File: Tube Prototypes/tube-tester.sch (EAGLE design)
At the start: 32 parts, among them IC1 NE555D, IC2 74141N, IC3 7805, Q1 IRF740S, Q2 BC546

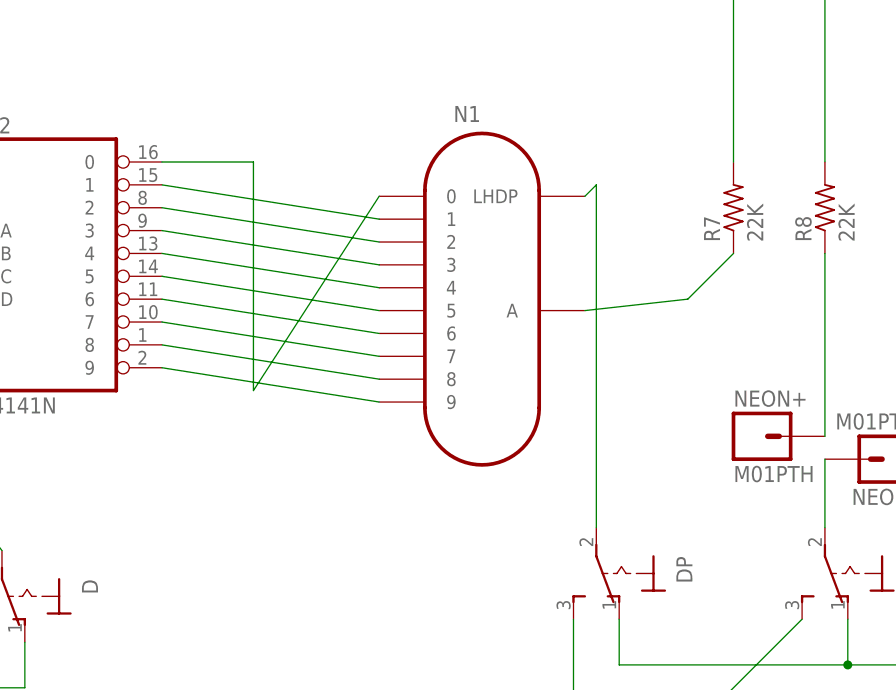
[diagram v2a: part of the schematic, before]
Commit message: new prototype for dual tube board
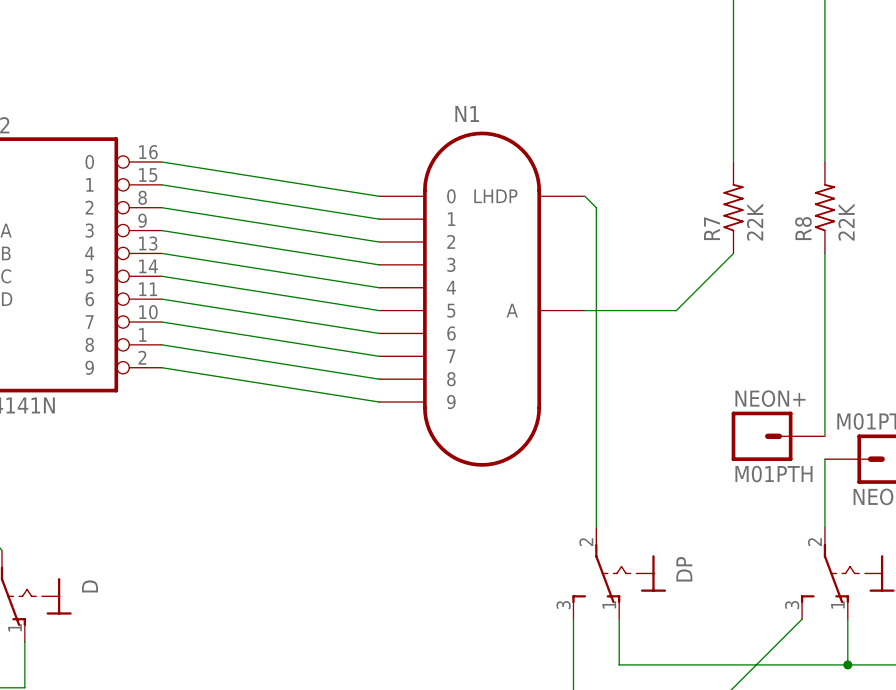
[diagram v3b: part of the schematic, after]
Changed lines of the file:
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@@
 <?xml version="1.0" encoding="utf-8"?>
 <!DOCTYPE eagle SYSTEM "eagle.dtd">
-<eagle version="6.4">
+<eagle version="6.6.0">
 <drawing>
 <settings>
@@
 <grid distance="0.05" unitdist="inch" unit="inch" style="lines" multiple="1" display="yes" altdistance="0.025" altunitdist="inch" altunit="inch"/>
 <layers>
-<layer number="1" name="Top" color="4" fill="1" visible="yes" active="no"/>
-<layer number="2" name="Route2" color="1" fill="3" visible="yes" active="no"/>
-<layer number="3" name="Route3" color="4" fill="3" visible="yes" active="no"/>
-<layer number="14" name="Route14" color="1" fill="6" visible="yes" active="no"/>
-<layer number="15" name="Route15" color="4" fill="6" visible="yes" active="no"/>
-<layer number="16" name="Bottom" color="1" fill="1" visible="yes" active="no"/>
-<layer number="17" name="Pads" color="2" fill="1" visible="yes" active="no"/>
-<layer number="18" name="Vias" color="2" fill="1" visible="yes" active="no"/>
-<layer number="19" name="Unrouted" color="6" fill="1" visible="yes" active="no"/>
-<layer number="20" name="Dimension" color="15" fill="1" visible="yes" active="no"/>
-<layer number="21" name="tPlace" color="7" fill="1" visible="yes" active="no"/>
-<layer number="22" name="bPlace" color="7" fill="1" visible="yes" active="no"/>
-<layer number="23" name="tOrigins" color="15" fill="1" visible="yes" active="no"/>
-<layer number="24" name="bOrigins" color="15" fill="1" visible="yes" active="no"/>
-<layer number="25" name="tNames" color="7" fill="1" visible="yes" active="no"/>
-<layer number="26" name="bNames" color="7" fill="1" visible="yes" active="no"/>
-<layer number="27" name="tValues" color="7" fill="1" visible="yes" active="no"/>
-<layer number="28" name="bValues" color="7" fill="1" visible="yes" active="no"/>
+<layer number="1" name="Top" color="4" fill="1" visible="no" active="no"/>
+<layer number="2" name="Route2" color="1" fill="3" visible="no" active="no"/>
+<layer number="3" name="Route3" color="4" fill="3" visible="no" active="no"/>
+<layer number="14" name="Route14" color="1" fill="6" visible="no" active="no"/>
+<layer number="15" name="Route15" color="4" fill="6" visible="no" active="no"/>
+<layer number="16" name="Bottom" color="1" fill="1" visible="no" active="no"/>
+<layer number="17" name="Pads" color="2" fill="1" visible="no" active="no"/>
+<layer number="18" name="Vias" color="2" fill="1" visible="no" active="no"/>
+<layer number="19" name="Unrouted" color="6" fill="1" visible="no" active="no"/>
+<layer number="20" name="Dimension" color="15" fill="1" visible="no" active="no"/>
+<layer number="21" name="tPlace" color="7" fill="1" visible="no" active="no"/>
+<layer number="22" name="bPlace" color="7" fill="1" visible="no" active="no"/>
+<layer number="23" name="tOrigins" color="15" fill="1" visible="no" active="no"/>
+<layer number="24" name="bOrigins" color="15" fill="1" visible="no" active="no"/>
+<layer number="25" name="tNames" color="7" fill="1" visible="no" active="no"/>
+<layer number="26" name="bNames" color="7" fill="1" visible="no" active="no"/>
+<layer number="27" name="tValues" color="7" fill="1" visible="no" active="no"/>
+<layer number="28" name="bValues" color="7" fill="1" visible="no" active="no"/>
 <layer number="29" name="tStop" color="7" fill="3" visible="no" active="no"/>
 <layer number="30" name="bStop" color="7" fill="6" visible="no" active="no"/>
@@
 <layer number="35" name="tGlue" color="7" fill="4" visible="no" active="no"/>
 <layer number="36" name="bGlue" color="7" fill="5" visible="no" active="no"/>
-<layer number="37" name="tTest" color="7" fill="1" visible="yes" active="no"/>
-<layer number="38" name="bTest" color="7" fill="1" visible="yes" active="no"/>
+<layer number="37" name="tTest" color="7" fill="1" visible="no" active="no"/>
+<layer number="38" name="bTest" color="7" fill="1" visible="no" active="no"/>
 <layer number="39" name="tKeepout" color="4" fill="11" visible="no" active="no"/>
 <layer number="40" name="bKeepout" color="1" fill="11" visible="no" active="no"/>
@@
 <layer number="44" name="Drills" color="7" fill="1" visible="no" active="no"/>
 <layer number="45" name="Holes" color="7" fill="1" visible="no" active="no"/>
-<layer number="46" name="Milling" color="3" fill="1" visible="yes" active="no"/>
-<layer number="47" name="Measures" color="7" fill="1" visible="yes" active="no"/>
-<layer number="48" name="Document" color="7" fill="1" visible="yes" active="no"/>
-<layer number="49" name="Reference" color="7" fill="1" visible="yes" active="no"/>
-<layer number="50" name="dxf" color="7" fill="1" visible="yes" active="no"/>
-<layer number="51" name="tDocu" color="7" fill="1" visible="yes" active="no"/>
-<layer number="52" name="bDocu" color="7" fill="1" visible="yes" active="no"/>
-<layer number="53" name="tGND_GNDA" color="7" fill="9" visible="yes" active="no"/>
-<layer number="54" name="bGND_GNDA" color="1" fill="9" visible="yes" active="no"/>
-<layer number="56" name="wert" color="7" fill="1" visible="yes" active="no"/>
+<layer number="46" name="Milling" color="3" fill="1" visible="no" active="no"/>
+<layer number="47" name="Measures" color="7" fill="1" visible="no" active="no"/>
+<layer number="48" name="Document" color="7" fill="1" visible="no" active="no"/>
+<layer number="49" name="Reference" color="7" fill="1" visible="no" active="no"/>
+<layer number="50" name="dxf" color="7" fill="1" visible="no" active="no"/>
+<layer number="51" name="tDocu" color="7" fill="1" visible="no" active="no"/>
+<layer number="52" name="bDocu" color="7" fill="1" visible="no" active="no"/>
+<layer number="53" name="tGND_GNDA" color="7" fill="9" visible="no" active="no"/>
+<layer number="54" name="bGND_GNDA" color="1" fill="9" visible="no" active="no"/>
+<layer number="56" name="wert" color="7" fill="1" visible="no" active="no"/>
 <layer number="91" name="Nets" color="2" fill="1" visible="yes" active="yes"/>
 <layer number="92" name="Busses" color="1" fill="1" visible="yes" active="yes"/>
@@
 </segment>
 </net>
-<net name="N$20" class="0">
-<segment>
-<pinref part="N1" gate="G$1" pin="0"/>
-<wire x1="214.63" y1="72.39" x2="200.66" y2="50.8" width="0.1524" layer="91"/>
-<wire x1="200.66" y1="50.8" x2="200.66" y2="76.2" width="0.1524" layer="91"/>
-<pinref part="IC2" gate="A" pin="0"/>
-<wire x1="200.66" y1="76.2" x2="190.5" y2="76.2" width="0.1524" layer="91"/>
-</segment>
-</net>
-<net name="N$21" class="0">
-<segment>
-<pinref part="R7" gate="G$1" pin="1"/>
-<pinref part="N1" gate="G$1" pin="A"/>
-<wire x1="254" y1="66.04" x2="248.92" y2="60.96" width="0.1524" layer="91"/>
-<wire x1="248.92" y1="60.96" x2="237.49" y2="59.69" width="0.1524" layer="91"/>
-</segment>
-</net>
 <net name="N$22" class="0">
 <segment>
@@
 </segment>
 </net>
+<net name="N$20" class="0">
+<segment>
+<pinref part="N1" gate="G$1" pin="0"/>
+<pinref part="IC2" gate="A" pin="0"/>
+<wire x1="214.63" y1="72.39" x2="190.5" y2="76.2" width="0.1524" layer="91"/>
+</segment>
+</net>
 <net name="N$30" class="0">
 <segment>
+<pinref part="DP" gate="1" pin="P"/>
 <pinref part="N1" gate="G$1" pin="LHDP"/>
-<pinref part="DP" gate="1" pin="P"/>
-<wire x1="237.49" y1="72.39" x2="238.76" y2="73.66" width="0.1524" layer="91"/>
-<wire x1="238.76" y1="73.66" x2="238.76" y2="35.56" width="0.1524" layer="91"/>
-</segment>
-</net>
+<wire x1="238.76" y1="35.56" x2="238.76" y2="71.12" width="0.1524" layer="91"/>
+<wire x1="238.76" y1="71.12" x2="237.49" y2="72.39" width="0.1524" layer="91"/>
+</segment>
+</net>
+<net name="N$21" class="0">
+<segment>
+<pinref part="R7" gate="G$1" pin="1"/>
+<pinref part="N1" gate="G$1" pin="A"/>
+<wire x1="254" y1="66.04" x2="247.65" y2="59.69" width="0.1524" layer="91"/>
+<wire x1="247.65" y1="59.69" x2="237.49" y2="59.69" width="0.1524" layer="91"/>
+</segment>
+</net>
